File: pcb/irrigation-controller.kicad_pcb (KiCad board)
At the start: 2 copper layers, 56 x 65 mm, 32 parts, among them J1 ZL262-40DG, J2 KFG-2EDGR-5.08-9P, Q1 PMBT3904, Q2 SS8550-H, Q3 PMBT3904, Q4 SS8550-H, Q5 PMBT3904, Q6 SS8550-H, Q7 PMBT3904, Q8 SS8550-H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

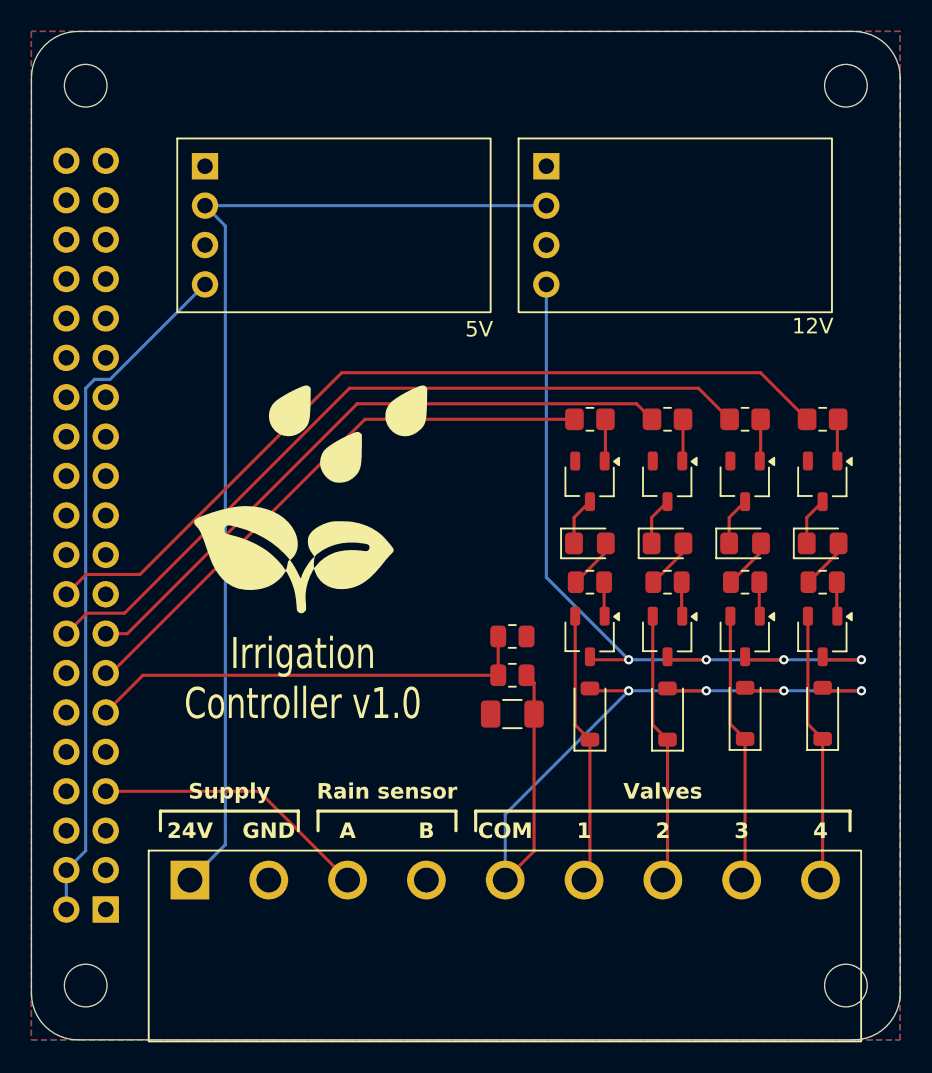
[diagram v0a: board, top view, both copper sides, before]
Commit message: Change terminal, add another output, add hardware debouncing
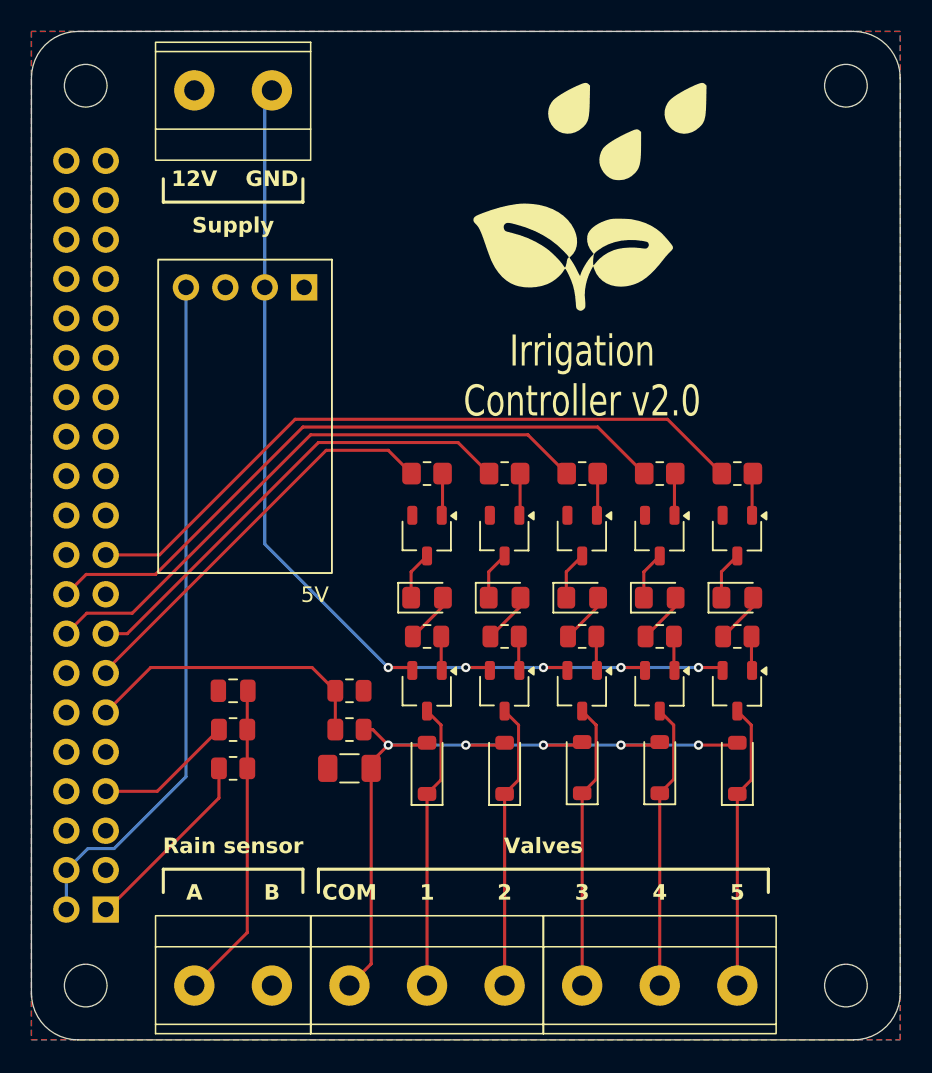
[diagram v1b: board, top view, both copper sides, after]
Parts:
- removed X2: 12V, Irrigation_Controller:STDN-3A24-ADJ
- added C1: 0.1 µF, Capacitor_SMD:C_0805_2012Metric, F.Cu at (158.0, 116.5)
- added D10: SD103AW, Diode_SMD:D_SOD-123, F.Cu at (190.5, 121.5)
- added D9: EVL-SMD0805-RED, LED_SMD:LED_0805_2012Metric_Pad1.15x1.40mm_HandSolder, F.Cu at (190.5, 110.5)
- added J3: Screw_Terminal_01x02, Irrigation_Controller:MX5-2P-BK, F.Cu at (155.5, 135.5)
- added J4: Screw_Terminal_01x03, Irrigation_Controller:MX5-3P-BK, F.Cu at (165.5, 135.5)
- added J5: Screw_Terminal_01x03, Irrigation_Controller:MX5-3P-BK, F.Cu at (180.5, 135.5)
- added Q10: SS8550-H, Package_TO_SOT_SMD:TSOT-23, F.Cu at (190.5, 116.5)
- added Q9: PMBT3904, Package_TO_SOT_SMD:TSOT-23, F.Cu at (190.5, 106.5)
- added R10: 620, Resistor_SMD:R_0805_2012Metric, F.Cu at (190.5, 113.0)
- added R13: 1.1K, Resistor_SMD:R_0805_2012Metric, F.Cu at (158.0, 119.0)
- added R14: 3.9K, Resistor_SMD:R_0805_2012Metric, F.Cu at (158.0, 121.5)
- added R9: 3.9K, Resistor_SMD:R_0805_2012Metric_Pad1.20x1.40mm_HandSolder, F.Cu at (190.5, 102.5)
- J2: value KFG-2EDGR-5.08-9P -> Screw_Terminal_01x02; footprint Irrigation_Controller:KFG-2EDGR-5.08-9P -> Irrigation_Controller:MX5-2P-BK
- R1, R3, R5, R7: value 4.3K -> 3.9K
- R11: renamed from R9; value 4.3K -> 3.9K
- R12: renamed from R10; value 1.5K -> 1.1K
- moved J2 51.2 mm to (160.5, 77.8), turned to 180 degrees
- moved G*** 26.5 mm to (181.0, 84.5)
- moved D1 11.1 mm to (170.5, 110.5)
- moved D2 11.1 mm to (170.5, 121.5)
- moved D3 11.1 mm to (175.5, 110.5)
- moved D4 11.1 mm to (175.5, 121.5)
- moved D5 11.1 mm to (180.5, 110.5)
- moved D6 11.1 mm to (180.5, 121.5)
- moved D7 11.1 mm to (185.5, 110.5)
- moved D8 11.1 mm to (185.5, 121.5)
- moved F1 11.1 mm to (165.5, 121.5)
- moved Q1 11.1 mm to (170.5, 106.5)
- moved Q2 11.1 mm to (170.5, 116.5)
- moved Q3 11.1 mm to (175.5, 106.5)
- moved Q4 11.1 mm to (175.5, 116.5)
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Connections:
- J1 pad 1: unconnected-(J1-3.3V-Pad1) -> +3V3
- J1 pad 19: unconnected-(J1-GPIO10-Pad19) -> /C5
- J2 pad 1: +24V -> +12V
- Q2 pad 2: /Valve #1/OUT -> +12V
- Q2 pad 3: +12V -> /Valve #1/OUT
- Q4 pad 2: /Valve #2/OUT -> +12V
- Q4 pad 3: +12V -> /Valve #2/OUT
- Q6 pad 2: /Valve #3/OUT -> +12V
- Q6 pad 3: +12V -> /Valve #3/OUT
- Q8 pad 2: /Valve #4/OUT -> +12V
- Q8 pad 3: +12V -> /Valve #4/OUT
- X1 pad 2: +24V -> +12V
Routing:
- net +24V: track 67.0 -> 0.00 mm
- net /C5: track 0.00 -> 44.8 mm
- net Net-(J3-Pin_1): track 0.00 -> 20.5 mm
- net /Valve #5/OUT: track 0.00 -> 18.4 mm
- net +12V: track 51.7 -> 68.8 mm, vias 4 -> 5
- net +3V3: track 0.00 -> 12.2 mm
- net /C4: track 54.9 -> 43.0 mm
- net /C3: track 50.1 -> 38.6 mm
- net /C2: track 41.8 -> 30.6 mm
- net /C1: track 37.0 -> 26.4 mm
- net /SHORT: track 28.8 -> 19.1 mm
- net /RAIN: track 18.0 -> 8.95 mm
- net Net-(D9-A): track 0.00 -> 3.30 mm
- net Net-(D9-K): track 0.00 -> 3.11 mm
- net Net-(Q9-B): track 0.00 -> 2.71 mm
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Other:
- board text added: "12V"
- board text added: "5"
- board text added: "Irrigation Controller v2.0"
- board text removed: "24V"
- board text removed: "Irrigation Controller v1.0"
